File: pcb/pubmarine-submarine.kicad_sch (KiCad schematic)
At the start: 101 parts, among them J1 Screw_Terminal_01x02, J10 Conn_01x02, J11 Conn_01x02, J12 Screw_Terminal_01x02, J13 Conn_01x03, J14 Conn_01x04, J15 Servo1, J16 Servo2, J17 Servo3, J18 Servo4, J19 Conn_01x02, J2 Conn_01x02, J20 Conn_01x02, J21 Conn_01x02, J22 Conn_01x02, J23 Conn_01x02, J24 Conn_01x02, J25 Conn_01x20, J26 Conn_01x20, J27 Conn_01x03, J3 Conn_01x02, J4 Conn_01x02, J5 Conn_01x02, J6 Screw_Terminal_01x02, J7 Screw_Terminal_01x02, J8 Conn_01x02, J9 Conn_01x02, Q1 AO3400A, Q2 AO3400A, Q3 AO3400A, Q4 AO3400A, Q5 AO3400A, Q6 AO3400A, Q7 AO3400A, Q8 AO3400A, SW1 SW_SPDT, SW2 SW_SPDT, U1 Pico, U2 SN74LV1T34DBV, U3 A4950E, U4 A4950E, U5 A4950E, U6 A4950E

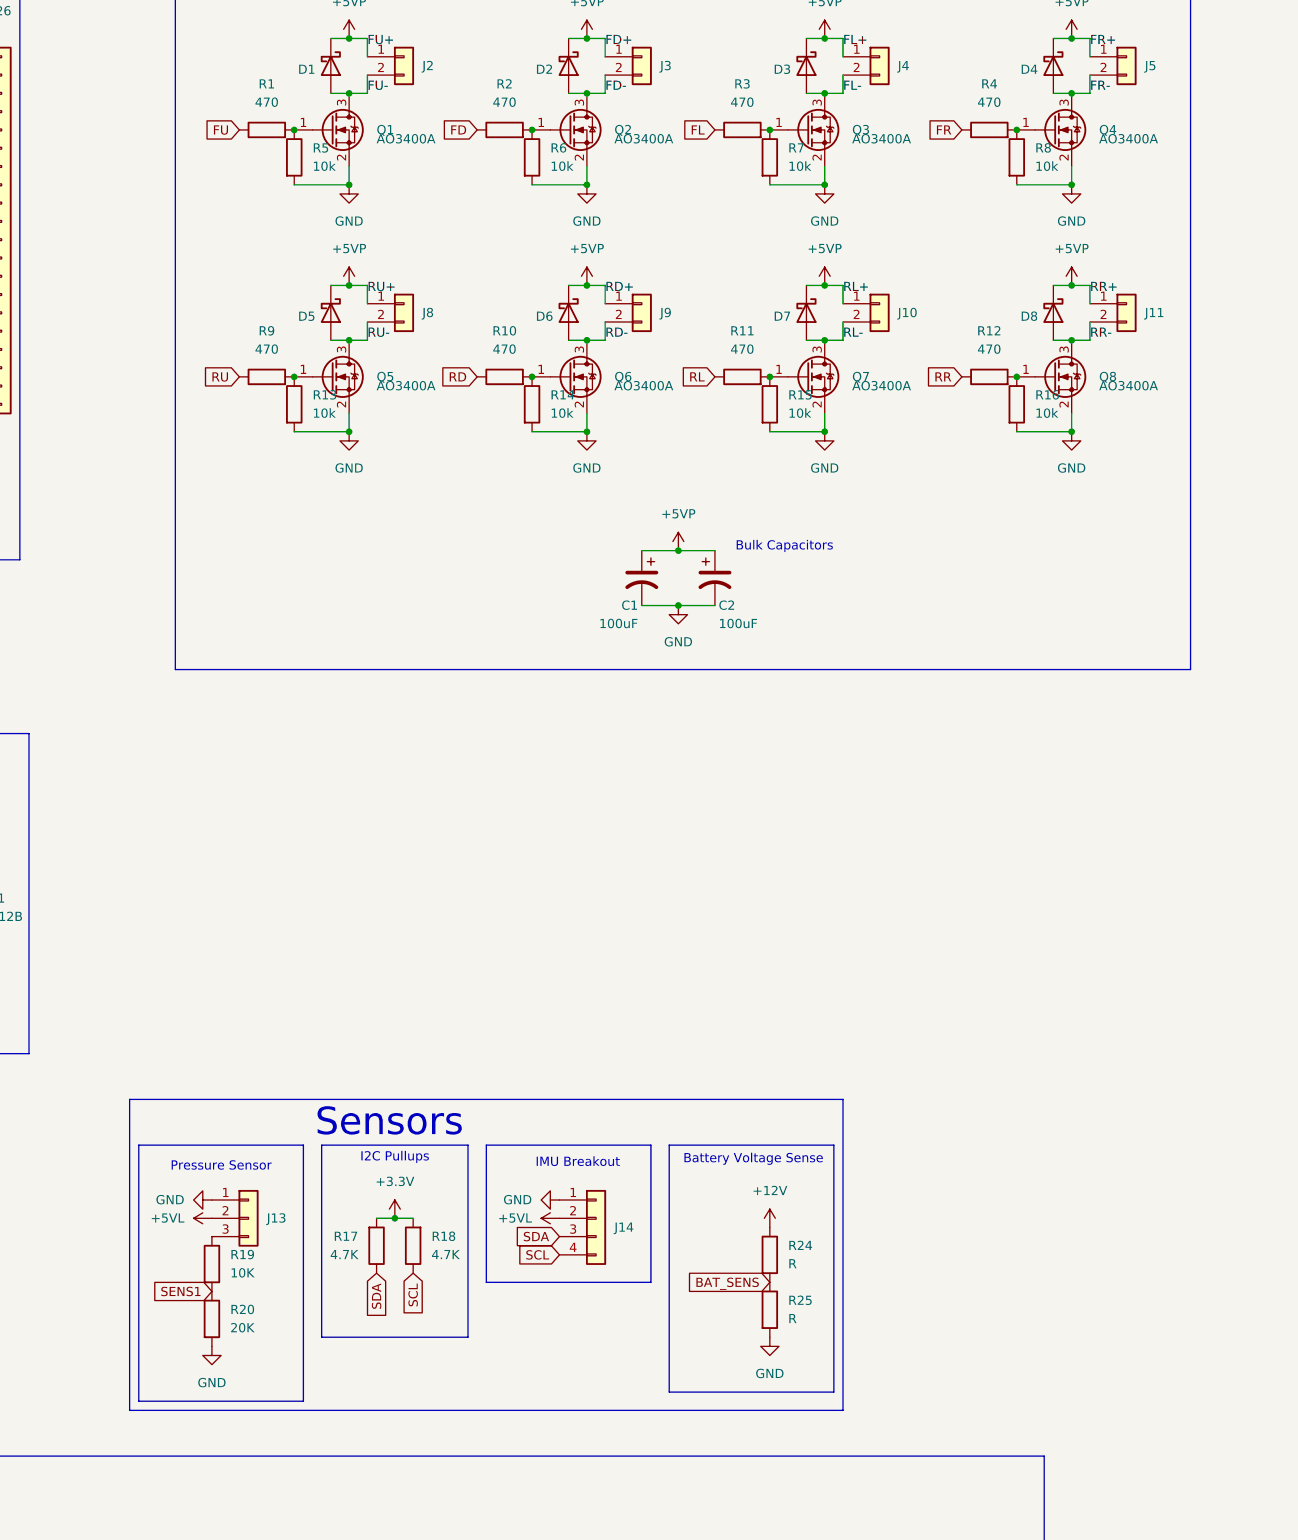
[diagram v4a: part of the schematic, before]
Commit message: pcb: IMU breakout and silkscreen cleanup
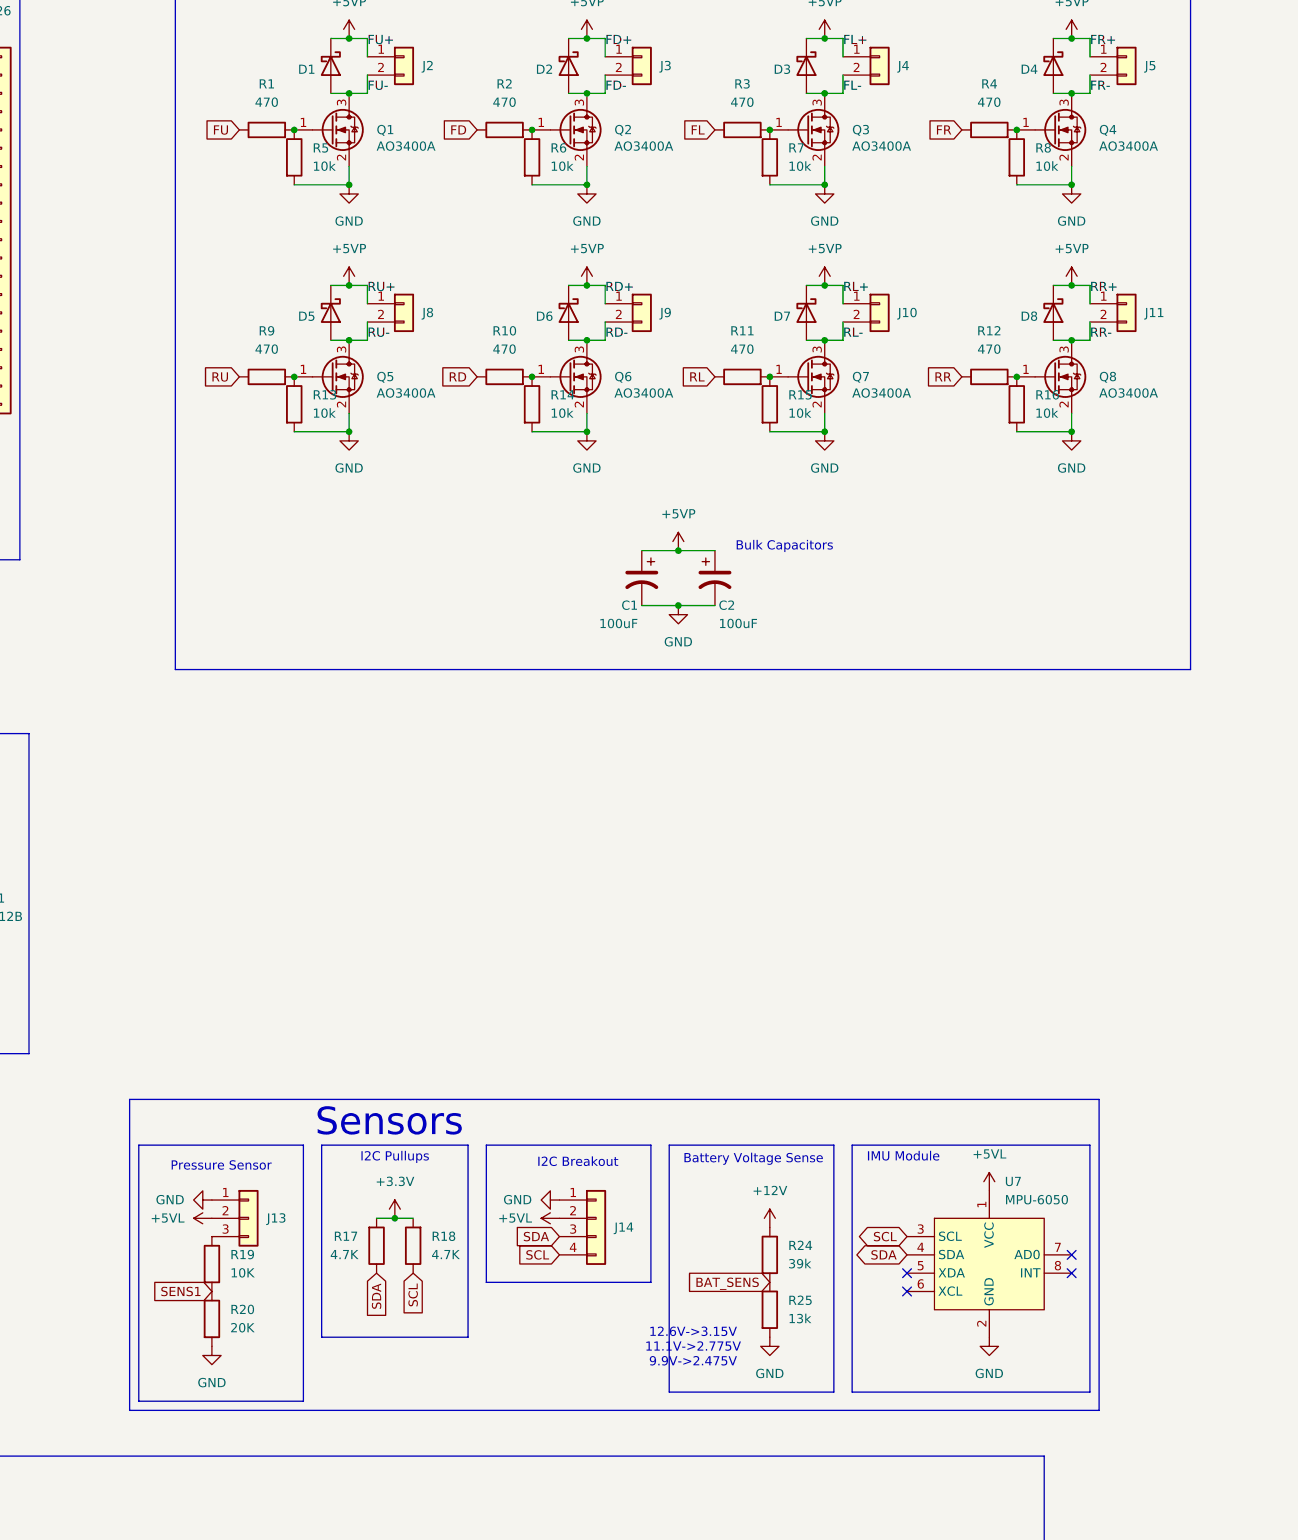
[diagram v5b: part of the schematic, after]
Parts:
- added U7: MPU-6050, pubmarine-submarine:MPU-6050_Module, symbol pubmarine-submarine:MPU-6050_Module
- R24: value R -> 39k
- R25: value R -> 13k
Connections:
- net +5VL: now also U7.1 (VCC)
- net GND: now also U7.2 (GND)
- net SCL: now also U7.3 (SCL)
- net SDA: now also U7.4 (SDA)
- no-connect marks 7 -> 11
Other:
- note added: "12.6V->3.15V 11.1V->2.775V 9.9V->2.475V"
- note added: "I2C Breakout"
- note added: "IMU Module"
- note removed: "IMU Breakout"

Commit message: silkscreen updates
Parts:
- C1, C11, C2, C5, C7, C9: value 100uF -> 100u
- C10, C4, C6, C8: value 0.22uF -> 220n
- C3: value 0.1uF -> 100n
- R1, R10, R11, R12, R2, R3, R4, R9: value 470 -> 470R
- R17, R18: value 4.7K -> 4k7
- R19: value 10K -> 10k
- R20: value 20K -> 20k
- R21: value 1K -> 1k
- R22, R23, R26: value 330 -> 330R
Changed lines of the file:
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@@
 	)
 	(rectangle
-		(start 20.32 189.23)
+		(start 19.05 189.23)
 		(end 104.14 215.9)
 		(stroke
@@
 			)
 		)
-		(property "Value" "0.22uF"
+		(property "Value" "220n"
 			(at 142.748 267.97 0)
 			(effects
@@
 			)
 		)
-		(property "Value" "100uF"
+		(property "Value" "100u"
 			(at 30.988 267.97 0)
 			(effects
@@
 			)
 		)
-		(property "Value" "470"
+		(property "Value" "470R"
 			(at 254 78.74 90)
 			(effects
@@
 			)
 		)
-		(property "Value" "0.1uF"
+		(property "Value" "100n"
 			(at 25.4 140.9699 0)
 			(effects
@@
 			)
 		)
-		(property "Value" "470"
+		(property "Value" "470R"
 			(at 153.67 78.74 90)
 			(effects
@@
 			)
 		)
-		(property "Value" "470"
+		(property "Value" "470R"
 			(at 219.71 44.45 90)
 			(effects
@@
 			)
 		)
-		(property "Value" "470"
+		(property "Value" "470R"
 			(at 186.69 78.74 90)
 			(effects
@@
 			)
 		)
-		(property "Value" "4.7K"
+		(property "Value" "4k7"
 			(at 176.53 204.4699 0)
 			(effects
@@
 			)
 		)
-		(property "Value" "470"
+		(property "Value" "470R"
 			(at 254 44.45 90)
 			(effects
@@
 		(fields_autoplaced yes)
 		(property "Reference" "R21"
-			(at 368.2999 45.72 0)
+			(at 369.57 36.83 90)
 			(effects
 				(font
 					(size 1.27 1.27)
 				)
-				(justify left)
 			)
 		)
-		(property "Value" "1K"
-			(at 370.8399 45.72 0)
+		(property "Value" "1k"
+			(at 369.57 39.37 90)
 			(effects
 				(font
 					(size 1.27 1.27)
 				)
-				(justify left)
 			)
 		)
@@
 			)
 		)
-		(property "Value" "100uF"
+		(property "Value" "100u"
 			(at 216.408 116.84 0)
 			(effects
@@
 			)
 		)
-		(property "Value" "100uF"
+		(property "Value" "100u"
 			(at 212.598 267.97 0)
 			(effects
@@
 			)
 		)
-		(property "Value" "470"
+		(property "Value" "470R"
 			(at 219.71 78.74 90)
 			(effects
@@
 		(fields_autoplaced yes)
 		(property "Reference" "R23"
-			(at 365.7599 106.68 0)
+			(at 367.03 97.79 90)
 			(effects
 				(font
 					(size 1.27 1.27)
 				)
-				(justify left)
 			)
 		)
-		(property "Value" "330"
-			(at 368.2999 106.68 0)
+		(property "Value" "330R"
+			(at 367.03 100.33 90)
 			(effects
 				(font
 					(size 1.27 1.27)
 				)
-				(justify left)
 			)
 		)
@@
 			)
 		)
-		(property "Value" "10K"
+		(property "Value" "10k"
 			(at 148.59 207.0099 0)
 			(effects
@@
 			)
 		)
-		(property "Value" "100uF"
+		(property "Value" "100u"
 			(at 205.232 116.84 0)
 			(effects
@@
 			)
 		)
-		(property "Value" "470"
+		(property "Value" "470R"
 			(at 186.69 44.45 90)
 			(effects
@@
 			)
 		)
-		(property "Value" "0.22uF"
+		(property "Value" "220n"
 			(at 22.098 267.97 0)
 			(effects
@@
 			)
 		)
-		(property "Value" "470"
+		(property "Value" "470R"
 			(at 153.67 44.45 90)
 			(effects
@@
 			)
 		)
-		(property "Value" "100uF"
+		(property "Value" "100u"
 			(at 91.948 267.97 0)
 			(effects
@@
 			)
 		)
-		(property "Value" "20K"
+		(property "Value" "20k"
 			(at 148.59 214.6299 0)
 			(effects
@@
 		(on_board yes)
 		(dnp no)
-		(fields_autoplaced yes)
 		(property "Reference" "R26"
-			(at 394.97 118.1099 0)
+			(at 390.906 118.11 0)
 			(effects
 				(font
 					(size 1.27 1.27)
 				)
-				(justify left)
+				(justify right)
 			)
 		)
-		(property "Value" "330"
-			(at 394.97 120.6499 0)
+		(property "Value" "330R"
+			(at 390.906 120.65 0)
 			(effects
 				(font
 					(size 1.27 1.27)
 				)
-				(justify left)
+				(justify right)
 			)
 		)
@@
 			)
 		)
-		(property "Value" "100uF"
+		(property "Value" "100u"
 			(at 151.638 267.97 0)
 			(effects
@@
 			)
 		)
-		(property "Value" "0.22uF"
+		(property "Value" "220n"
 			(at 203.708 267.97 0)
 			(effects
@@
 		(fields_autoplaced yes)
 		(property "Reference" "R22"
-			(at 367.0299 74.93 0)
+			(at 368.3 66.04 90)
 			(effects
 				(font
 					(size 1.27 1.27)
 				)
-				(justify left)
 			)
 		)
-		(property "Value" "330"
-			(at 369.5699 74.93 0)
+		(property "Value" "330R"
+			(at 368.3 68.58 90)
 			(effects
 				(font
 					(size 1.27 1.27)
 				)
-				(justify left)
 			)
 		)
@@
 			)
 		)
-		(property "Value" "0.22uF"
+		(property "Value" "220n"
 			(at 83.058 267.97 0)
 			(effects
@@
 			)
 		)
-		(property "Value" "4.7K"
+		(property "Value" "4k7"
 			(at 166.37 204.4699 0)
 			(effects

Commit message: pcb update
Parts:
- removed D15, D16: LED, LED_SMD:LED_0603_1608Metric_Pad1.05x0.95mm_HandSolder, symbol Device:LED
- removed R26: 330R, Resistor_SMD:R_0603_1608Metric_Pad0.98x0.95mm_HandSolder, symbol Device:R
- removed R27: 1K, Resistor_SMD:R_0603_1608Metric_Pad0.98x0.95mm_HandSolder, symbol Device:R
- removed SW1, SW2: SW_SPDT, Button_Switch_THT:SW_Slide_SPDT_Straight_CK_OS102011MS2Q, symbol Switch:SW_SPDT
- added JP1: Jumper_2_Bridged, Jumper:SolderJumper-2_P1.3mm_Bridged_RoundedPad1.0x1.5mm, symbol Jumper:Jumper_2_Bridged
- D1, D2, D3, D4, D5, D6, D7, D8: value 1N5822 -> B5819W; footprint Diode_SMD:D_0603_1608Metric -> Diode_SMD:D_SOD-123
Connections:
- net LED_PWR is gone; now on net +12V: J23.1 (Pin_1), J24.1 (Pin_1)
- net PI_PWR is gone; now on net +5VL: J12.1 (Pin_1)
- net +5VL: now also JP1.2 (B); no longer J26.2 (Pin_2), U1.39 (VSYS)
- new net: J26.2 (Pin_2), JP1.1 (A), U1.39 (VSYS)
- no-connect marks 11 -> 9
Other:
- moved on the sheet: J12, J23

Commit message: pcb update
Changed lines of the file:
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@@
 	)
 	(junction
-		(at 109.22 48.26)
-		(diameter 0)
-		(color 0 0 0 0)
-	)
-	(junction
 		(at 151.13 250.19)
 		(diameter 0)
@@
 					(unit 1)
 				)
-			)
-		)
-	)
-	(symbol
-		(lib_id "power:PWR_FLAG")
-		(at 109.22 48.26 0)
-		(mirror y)
-		(unit 1)
-		(exclude_from_sim no)
-		(in_bom yes)
-		(on_board yes)
-		(dnp no)
-		(fields_autoplaced yes)
-		(property "Reference" "#FLG6"
-			(at 109.22 46.355 0)
-			(effects
-				(font
-					(size 1.27 1.27)
-				)
-				(hide yes)
-			)
-		)
-		(property "Value" "PWR_FLAG"
-			(at 109.22 43.18 0)
-			(effects
-				(font
-					(size 1.27 1.27)
-				)
-				(hide yes)
-			)
-		)
-		(property "Footprint" ""
-			(at 109.22 48.26 0)
-			(effects
-				(font
-					(size 1.27 1.27)
-				)
-				(hide yes)
-			)
-		)
-		(property "Datasheet" "~"
-			(at 109.22 48.26 0)
-			(effects
-				(font
-					(size 1.27 1.27)
-				)
-				(hide yes)
-			)
-		)
-		(property "Description" "Special symbol for telling ERC where power comes from"
-			(at 109.22 48.26 0)
-			(effects
-				(font
-					(size 1.27 1.27)
-				)
-				(hide yes)
-			)
-		)
-		(pin "1"
-		)
-		(instances
-			(project "pubmarine-submarine"
-				(path "/12d1b76a-b790-4941-94cf-e8b80e5b52d9"
-					(reference "#FLG6")
-					(unit 1)
-				)
